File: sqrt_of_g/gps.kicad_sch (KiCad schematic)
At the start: 14 parts, among them J1 Amphenol_901-144, J2 Amphenol_901-144, Q8 IRLML2803, Q9 NDS8434, U3 S1216V8, U4 EP2W+

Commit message: ready for 2nd round of reviews
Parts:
- removed C32: 10nF, symbol pycubed_mainboard:10NF_10000PF-50V-10%(0603)
- removed C50: 10uF, symbol pycubed_mainboard:10NF_10000PF-50V-10%(0603)
- removed C51: 4.7uF, symbol pycubed_mainboard:10NF_10000PF-50V-10%(0603)
- removed C52: 0.22uF, symbol pycubed_mainboard:10NF_10000PF-50V-10%(0603)
- removed Q8: IRLML2803, mainboard:SOT-23, symbol mainboard:IRLML2803TRPBF
- removed Q9: NDS8434, mainboard:NDS8434, symbol mainboard:NDS8434
- removed R13: 4.7K, Resistor_SMD:R_0603_1608Metric, symbol mainboard:R-US_R0603
- removed R14: 3.3K, Resistor_SMD:R_0603_1608Metric, symbol mainboard:R-US_R0603
- removed R3: 10K, Resistor_SMD:R_0603_1608Metric, symbol mainboard:R-US_R0603
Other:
- added sheet Enable (power_enable.kicad_sch)
- note removed: "GPS Power"
- moved on the sheet: R18, U3

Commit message: pete feedback
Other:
- company: (none) -> Stanford Student Space Initiative
- moved on the sheet: J1, J2, R18, U3, U4

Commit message: update board
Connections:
- net RX_GPS renamed RX_FROM_MICRO
- net TX_GPS renamed TX_TO_MICRO
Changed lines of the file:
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@@
     (effects (font (size 1.27 1.27)) (justify left bottom))
   )
-  (hierarchical_label "TX_GPS" (shape output) (at 132.6642 115.57 180) (fields_autoplaced)
+  (hierarchical_label "TX_TO_MICRO" (shape output) (at 132.6642 115.57 180) (fields_autoplaced)
     (effects (font (size 1.27 1.27)) (justify right))
   )
-  (hierarchical_label "RX_GPS" (shape input) (at 132.6642 118.11 180) (fields_autoplaced)
+  (hierarchical_label "RX_FROM_MICRO" (shape input) (at 132.6642 118.11 180) (fields_autoplaced)
     (effects (font (size 1.27 1.27)) (justify right))
   )

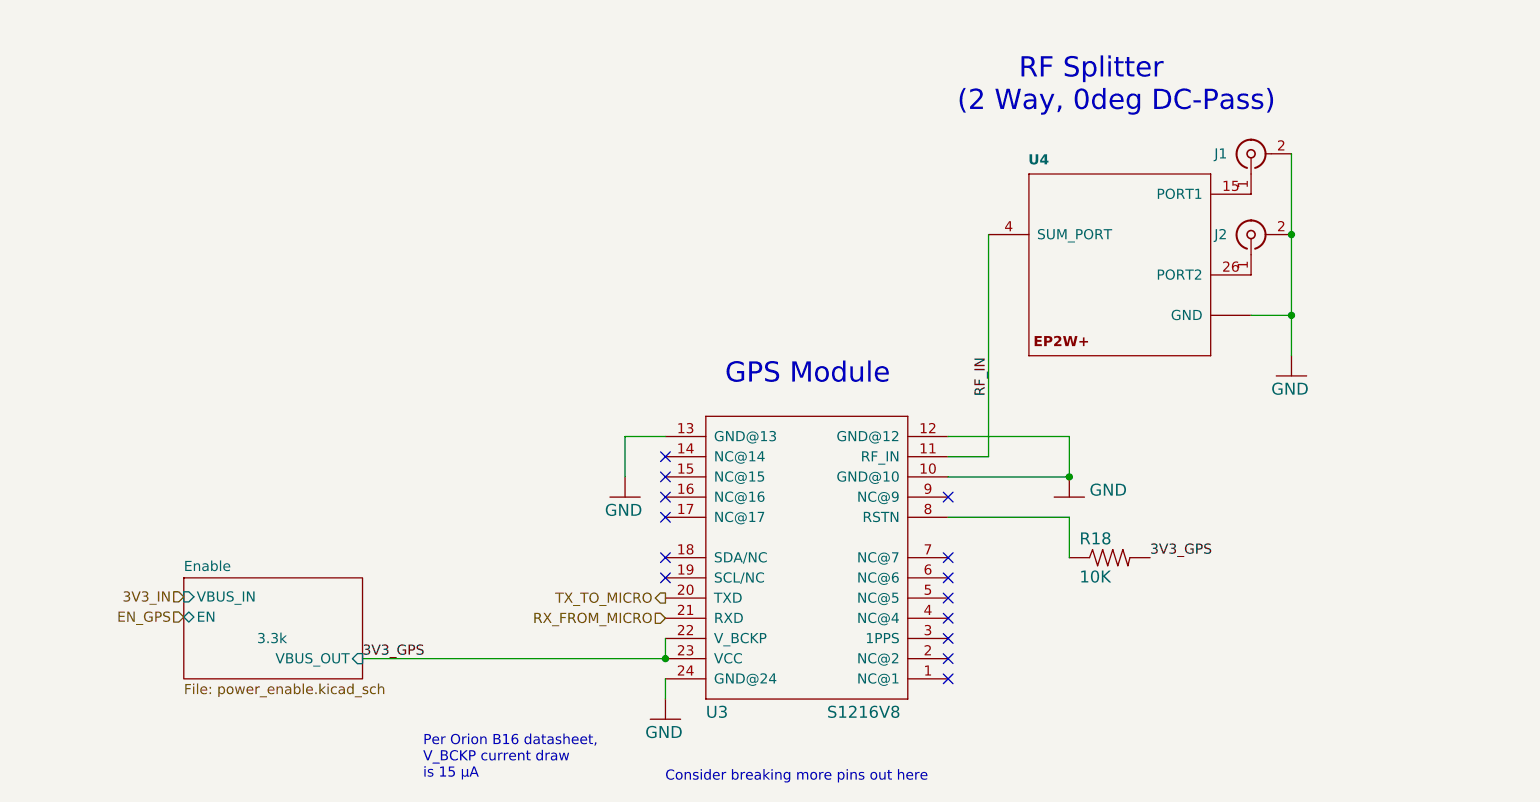
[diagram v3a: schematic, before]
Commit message: update gps schematic
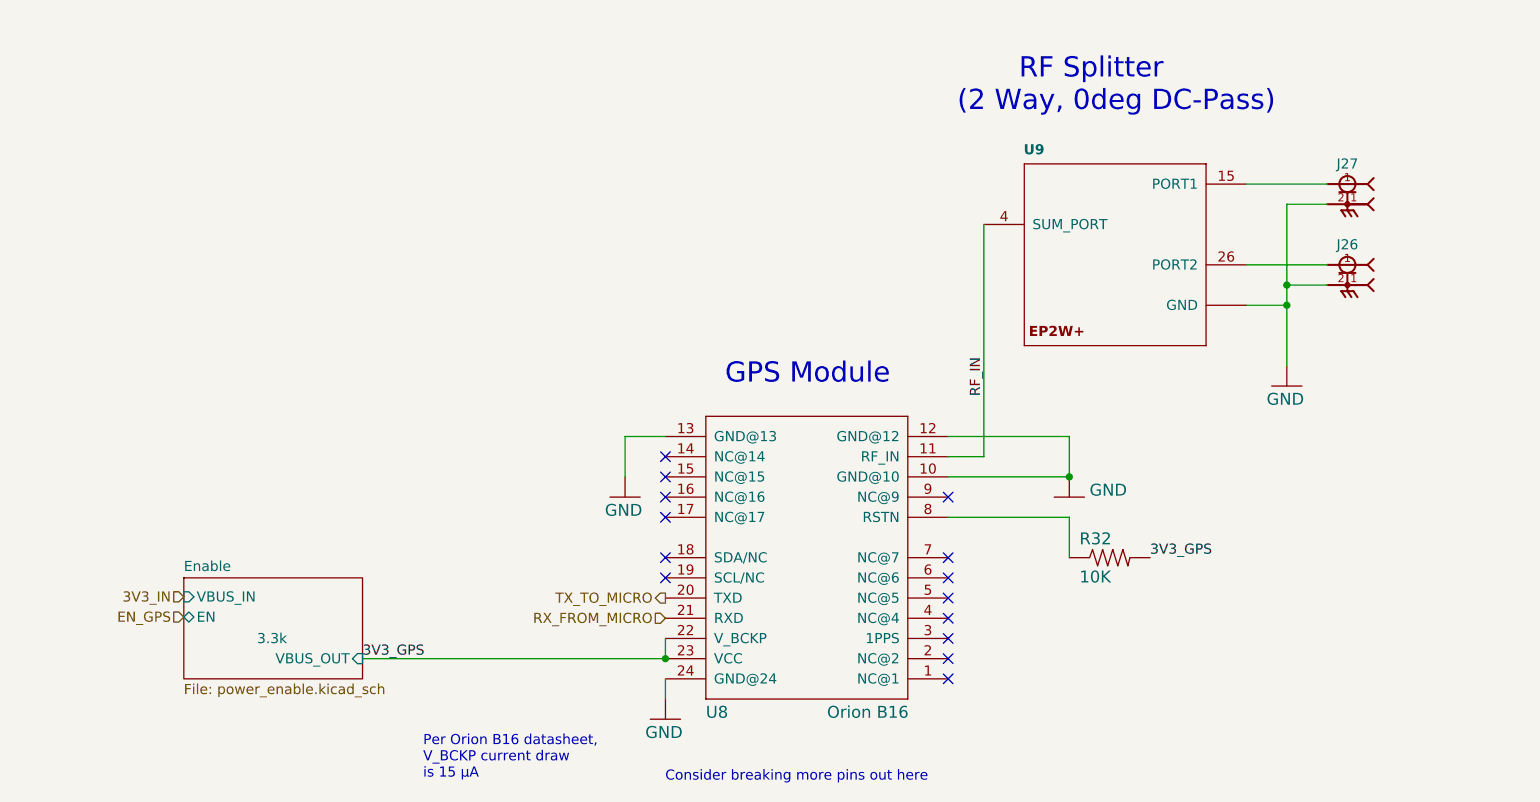
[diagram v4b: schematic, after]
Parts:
- removed J1, J2: Amphenol_901-144, mainboard:SMA_901-144-horizontal, symbol Connector:Conn_Coaxial
- added J26, J27: SMA-J-P-H-ST-EM1, SMA-J-P-H-ST-EM1:SAMTEC_SMA-J-P-H-ST-EM1, symbol adcs:SMA-J-P-H-ST-EM1
- U8: renamed from U3; value S1216V8 -> Orion B16; DNI (none) -> DNI; Flight (none) -> B16; Manufacturer_Name (none) -> SkyTraq; Unit Price (none) -> 850.0; Unit Price (Proto) (none) -> 6.80
- U9: renamed from U4; Manufacturer_Part_Number EP2W+ -> (none); Unit Price (none) -> 24.92
- renumbered R18 to R32
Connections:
- net GND: now also J26.2_1, J27.2_1
- net at U9.15 (PORT1): now also J27.1
- net at U9.26 (PORT2): now also J26.1
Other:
- moved on the sheet: U9
